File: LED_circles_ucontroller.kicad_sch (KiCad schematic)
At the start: 20 parts, among them J1 Conn_ARM_SWD_EDGE, U75 M95256-WMN6P, U76 M95256-WMN6P, U77 STM32G071KBTxN

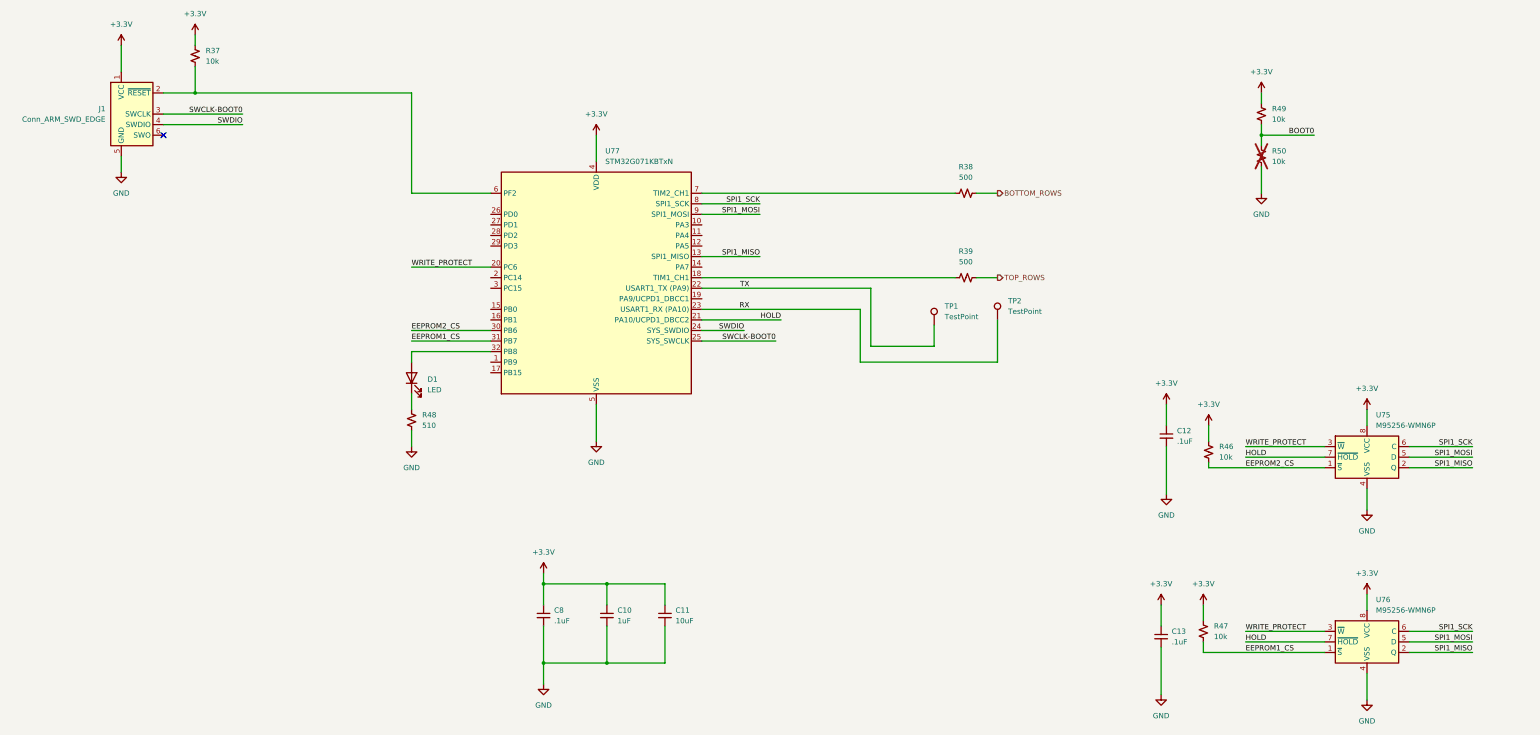
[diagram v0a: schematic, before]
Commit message: Fixed connectivity problems
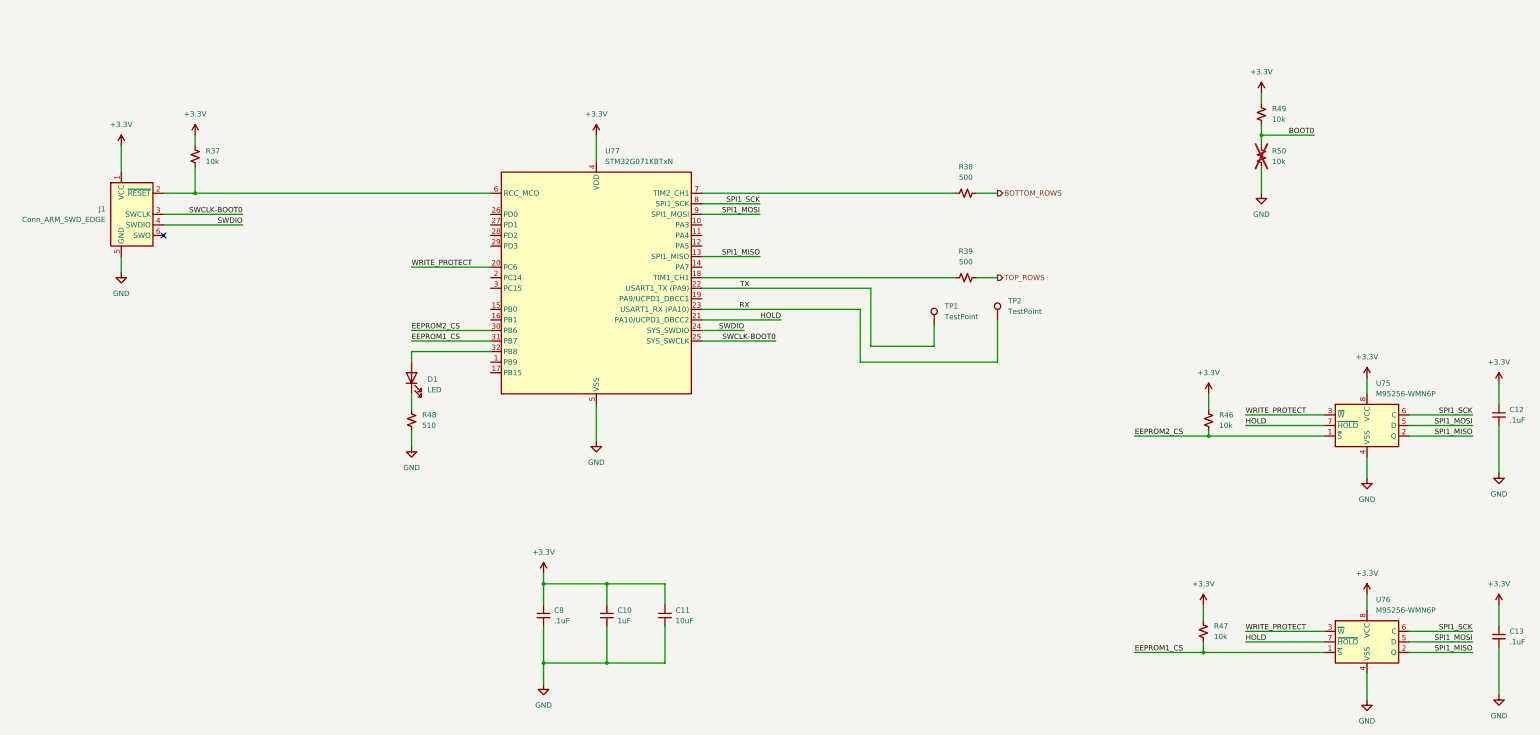
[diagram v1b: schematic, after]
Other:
- moved on the sheet: C12, C13, J1, R37, R46, U75
